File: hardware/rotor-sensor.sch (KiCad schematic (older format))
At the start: 35 parts, among them J1 Conn_01x03, J2 Conn_01x03, J3 Conn_01x03, U1 ATtiny202-SS, U2 EE-SX199, U3 SM351LT

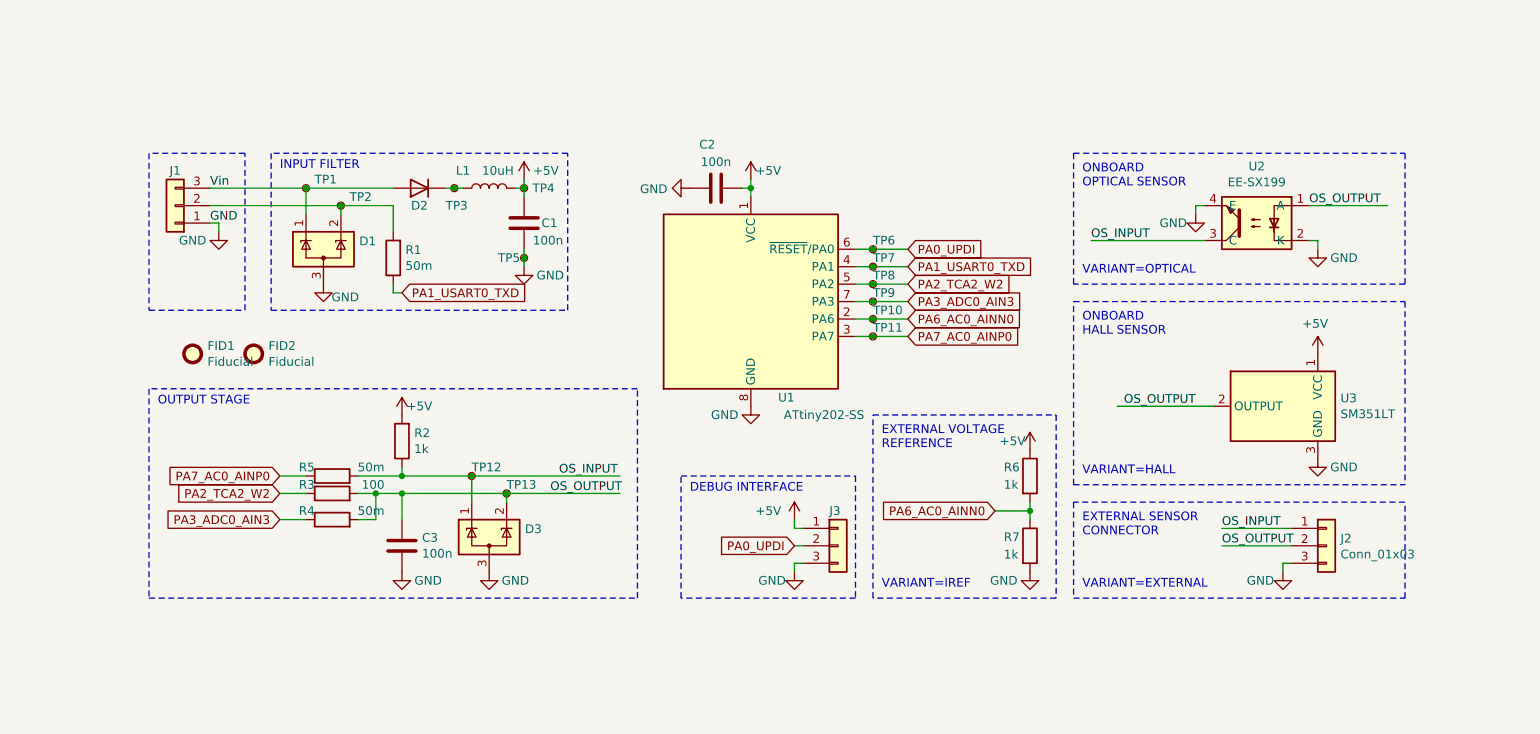
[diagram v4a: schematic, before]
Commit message: Adds LIN Transceiver to the design (#7)
Updates layout and schematic, replaced test point labels on schematic
Adds overcurrent protection IC and removes sense line

Hardware container version downgrade, KiKit downgrade
Hardware workflow retention day set to 5 days and
STEP generation step is skipped due to errors

Fixes track clearance issue on panelized layout
Tight frame and 1x4 panel layout
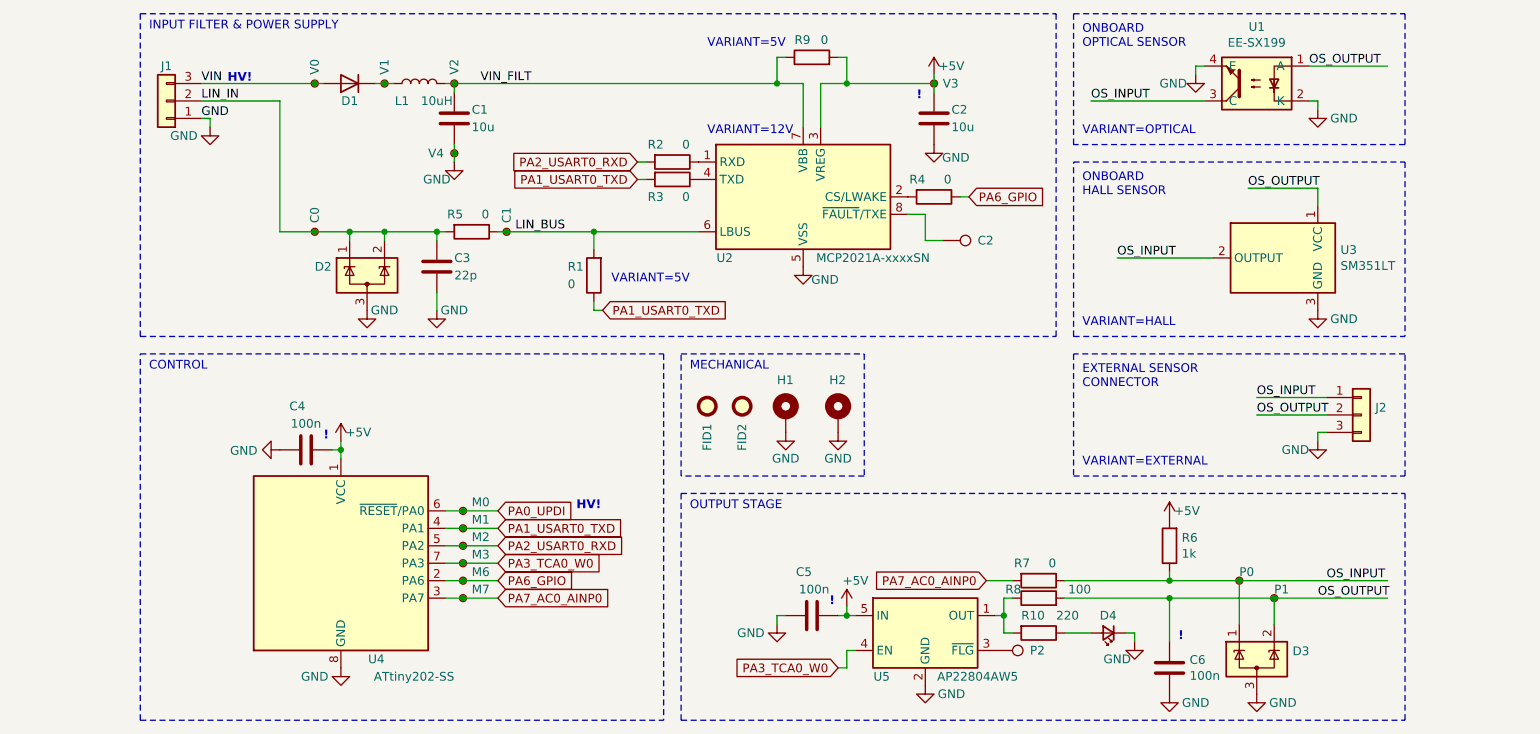
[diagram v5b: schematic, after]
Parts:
- removed J3: Conn_01x03, Connector_PinHeader_1.27mm:PinHeader_1x03_P1.27mm_Vertical, symbol Connector_Generic:Conn_01x03
- removed R5: 50m, Resistor_SMD:R_0603_1608Metric, symbol Device:R
- removed R6: 1k, Resistor_SMD:R_0603_1608Metric, symbol Device:R
- added C2: 10u, Capacitor_SMD:C_1206_3216Metric, symbol Device:C
- added C3: 22p, Capacitor_SMD:C_0603_1608Metric, symbol Device:C
- added C5: 100n, Capacitor_SMD:C_0603_1608Metric, symbol Device:C
- added D4: LED_Small, LED_SMD:LED_0603_1608Metric, symbol Device:LED_Small
- added H1, H2: MountingHole_Pad, MountingHole:MountingHole_2.2mm_M2_DIN965_Pad_TopOnly, symbol Mechanical:MountingHole_Pad
- added R1, R2, R3: 0, Resistor_SMD:R_0402_1005Metric, symbol Device:R
- added R10: 220, Resistor_SMD:R_0603_1608Metric, symbol Device:R
- added R9: 0, Resistor_SMD:R_0603_1608Metric, symbol Device:R
- added TP17: P2, TestPoint:TestPoint_Pad_D1.0mm, symbol Connector:TestPoint
- added TP4: V3, TestPoint:TestPoint_Pad_D1.0mm, symbol Connector:TestPoint_Small
- added TP7: C1, TestPoint:TestPoint_Pad_D1.0mm, symbol Connector:TestPoint_Small
- added TP8: C2, TestPoint:TestPoint_Pad_D1.0mm, symbol Connector:TestPoint
- added U2: MCP2021A-xxxxSN, Package_SO:SOIC-8_3.9x4.9mm_P1.27mm, symbol Interface_CAN_LIN:MCP2021A-xxxxSN
- added U5: AP22804AW5, Package_TO_SOT_SMD:SOT-23-5, symbol Power_Management:AP22804AW5
- C1: value 100n -> 10u; footprint Capacitor_SMD:C_0603_1608Metric -> Capacitor_SMD:C_1206_3216Metric
- J1: footprint Connector_PinHeader_2.54mm:PinHeader_1x03_P2.54mm_Vertical -> Connector_JST:JST_PH_B3B-PH-K_1x03_P2.00mm_Vertical
- R4: value 50m -> 0; footprint Resistor_SMD:R_0603_1608Metric -> Resistor_SMD:R_0402_1005Metric
- R5: renamed from R1; value 50m -> 0; footprint Resistor_SMD:R_0603_1608Metric -> Resistor_SMD:R_0402_1005Metric
- R7: value 1k -> 0; footprint Resistor_SMD:R_0603_1608Metric -> Resistor_SMD:R_0402_1005Metric; Config +IREF -> (none)
- TP1: value + -> V0
- TP10: renamed from TP7; value COMB -> M1
- TP11: renamed from TP8; value W2 -> M2
- TP12: renamed from TP9; value SENSE -> M3
- TP13: renamed from TP10; value AC- -> M6
- TP14: renamed from TP12; value IN -> P0
- TP15: renamed from TP11; value AC+ -> M7
- TP16: renamed from TP13; value OUT -> P1
- TP2: value COMA -> V1
- TP3: renamed from TP4; value VCC -> V2
- TP5: value - -> V4
- TP6: renamed from TP3; value VD -> C0
- TP9: renamed from TP6; value UPDI -> M0
- renumbered C2 to C4, C3 to C6, D2 to D1, D1 to D2, FID2 to FID1, FID1 to FID2, R2 to R6, R3 to R8, U2 to U1, U1 to U4
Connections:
- net labels added: LIN_BUS, LIN_IN, PA2_USART0_RXD, PA3_TCA0_W0, PA6_GPIO, VIN, VIN_FILT
- net labels removed: PA2_TCA2_W2, PA3_ADC0_AIN3, PA6_AC0_AINN0, Vin
- wire segments 68 -> 100
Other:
- note added: "!"
- note added: "CONTROL"
- note added: "HV!"
- note added: "INPUT FILTER & POWER SUPPLY"
- note added: "MECHANICAL"
- note added: "VARIANT=12V"
- note added: "VARIANT=5V"
- note removed: "DEBUG INTERFACE"
- note removed: "EXTERNAL VOLTAGE\nREFERENCE"
- note removed: "INPUT FILTER"
- note removed: "VARIANT=IREF"
- moved on the sheet: C1, C4, C6, D1, D2, D3, FID1, FID2, J1, J2, L1, R5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
